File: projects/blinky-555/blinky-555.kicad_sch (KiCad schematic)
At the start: 9 parts, among them J1 9-12V IN, U1 NE555P

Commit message: feat(P1-T9b): fixtures on the parts registry (pins by function, strict mode)
Co-Authored-By: Claude Opus 5.5 <noreply@anthropic.com>
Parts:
- C1: symbol Device:C -> Device:C_Polarized
- D1: LCSC C2895470 -> (none)
- U1: LCSC (none) -> C46749
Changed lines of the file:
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@@
+			)
+		)
+		(property "LCSC" "C46749"
+			(at 48.26 116.84 0)
+			(show_name no)
+			(do_not_autoplace no)
+			(hide yes)
+			(effects
+				(font
+					(size 1.27 1.27)
+				)
 			)
 		)
@@
 	(wire (pts (xy 88.9 115.57) (xy 88.9 118.11)) (stroke (width 0) (type default)))
 	(label "TRIG" (at 88.9 118.11 270) (effects (font (size 1.27 1.27)) (justify right bottom)))
-	(symbol (lib_id "Device:C") (at 101.6 111.76 0) (unit 1) (exclude_from_sim no) (in_bom yes) (on_board yes) (dnp no)
+	(symbol (lib_id "Device:C_Polarized") (at 101.6 111.76 0) (unit 1) (exclude_from_sim no) (in_bom yes) (on_board yes) (dnp no)
 		(property "Reference" "C1"
-			(at 104.902 110.49 0)
+			(at 105.156 110.49 0)
 			(show_name no)
 			(do_not_autoplace no)
@@
 		)
 		(property "Value" "10uF"
-			(at 104.902 113.03 0)
+			(at 105.156 113.03 0)
 			(show_name no)
 			(do_not_autoplace no)
@@
 			)
 		)
-		(property "Description" "Unpolarized capacitor"
+		(property "Description" "Polarized capacitor"
 			(at 101.6 111.76 0)
 			(show_name no)
@@
 			(at 50.8 170.18 0)
 			(show_name no)
-			(do_not_autoplace no)
-			(hide yes)
-			(effects
-				(font
-					(size 1.27 1.27)
-				)
-			)
-		)
-		(property "LCSC" "C2895470"
-			(at 50.8 170.18 0)
-			(show_name no)

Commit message: fix(P1-T9b): keep LCSC ids, package family match, PR-BYNAME
Co-Authored-By: Claude Opus 5.5 <noreply@anthropic.com>
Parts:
- D1: LCSC (none) -> C2895470
- U1: LCSC C46749 -> (none)
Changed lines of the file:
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@@
-			)
-		)
-		(property "LCSC" "C46749"
-			(at 48.26 116.84 0)
-			(show_name no)
-			(do_not_autoplace no)
-			(hide yes)
-			(effects
-				(font
-					(size 1.27 1.27)
-				)
 			)
 		)
@@
 			(at 50.8 170.18 0)
 			(show_name no)
+			(do_not_autoplace no)
+			(hide yes)
+			(effects
+				(font
+					(size 1.27 1.27)
+				)
+			)
+		)
+		(property "LCSC" "C2895470"
+			(at 50.8 170.18 0)
+			(show_name no)

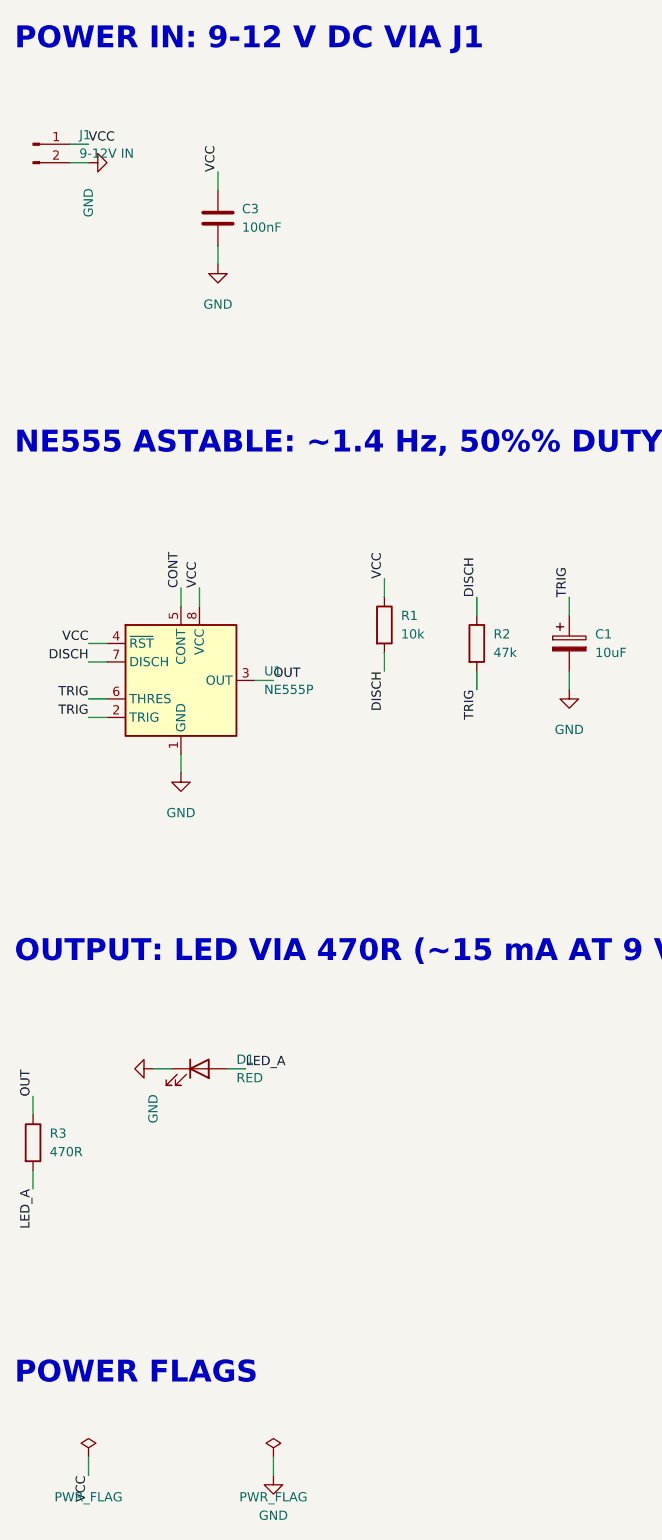
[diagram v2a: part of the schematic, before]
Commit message: feat(P2-T7b): RC-filter recognition, direction severities, expansion class; blinky reverse-polarity diode
Co-Authored-By: Claude Opus 5.5 <noreply@anthropic.com>
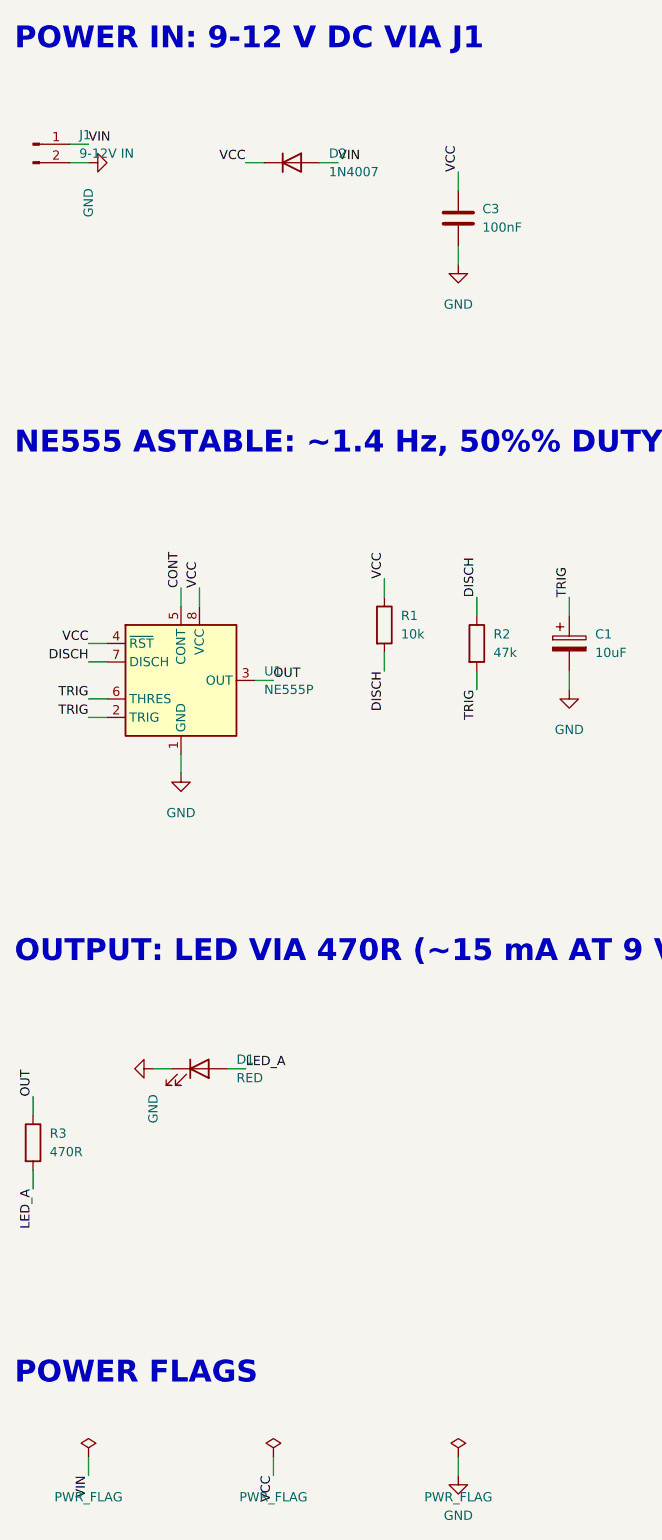
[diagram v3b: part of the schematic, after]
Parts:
- added D2: 1N4007, Diode_THT:D_DO-41_SOD81_P7.62mm_Horizontal, symbol Device:D
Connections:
- net VCC: now also D2.1 (K); no longer J1.1 (Pin_1)
- new net VIN: D2.2 (A), J1.1 (Pin_1)
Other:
- moved on the sheet: C3
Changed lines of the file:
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@@
 	)
 	(wire (pts (xy 33.02 43.18) (xy 35.56 43.18)) (stroke (width 0) (type default)))
-	(label "VCC" (at 35.56 43.18 0) (effects (font (size 1.27 1.27)) (justify left bottom)))
+	(label "VIN" (at 35.56 43.18 0) (effects (font (size 1.27 1.27)) (justify left bottom)))
 	(wire (pts (xy 33.02 45.72) (xy 35.56 45.72)) (stroke (width 0) (type default)))
 	(symbol (lib_id "power:GND") (at 35.56 45.72 90) (unit 1) (exclude_from_sim no) (in_bom no) (on_board yes) (dnp no)
@@
 		(instances (project "blinky-555" (path "/5f01663b-fc79-577d-9212-5270d9429f25" (reference "#PWR001") (unit 1))))
 	)
-	(symbol (lib_id "Device:C") (at 53.34 53.34 0) (unit 1) (exclude_from_sim no) (in_bom yes) (on_board yes) (dnp no)
+	(symbol (lib_id "Device:D") (at 63.5 45.72 0) (unit 1) (exclude_from_sim no) (in_bom yes) (on_board yes) (dnp no)
+		(property "Reference" "D2"
+			(at 68.58 44.45 0)
+			(show_name no)
+			(do_not_autoplace no)
+			(effects
+				(font
+					(size 1.27 1.27)
+				)
+				(justify left)
+			)
+		)
+		(property "Value" "1N4007"
+			(at 68.58 46.99 0)
+			(show_name no)
+			(do_not_autoplace no)
+			(effects
+				(font
+					(size 1.27 1.27)
+				)
+				(justify left)
+			)
+		)
+		(property "Footprint" "Diode_THT:D_DO-41_SOD81_P7.62mm_Horizontal"
+			(at 63.5 45.72 0)
+			(show_name no)
+			(do_not_autoplace no)
+			(hide yes)
+			(effects
+				(font
+					(size 1.27 1.27)
+				)
+			)
+		)
+		(property "Datasheet" ""
+			(at 63.5 45.72 0)
+			(show_name no)
+			(do_not_autoplace no)
+			(hide yes)
+			(effects
+				(font
+					(size 1.27 1.27)
+				)
+			)
+		)
+		(property "Description" "Diode"
+			(at 63.5 45.72 0)
+			(show_name no)
+			(do_not_autoplace no)
+			(hide yes)
+			(effects
+				(font
+					(size 1.27 1.27)
+				)
+			)
+		)
+		(property "Sim.Device" "D"
+			(at 63.5 45.72 0)
+			(show_name no)
+			(do_not_autoplace no)
+			(hide yes)
+			(effects
+				(font
+					(size 1.27 1.27)
+				)
+			)
+		)
+		(property "Sim.Pins" "1=K 2=A"
+			(at 63.5 45.72 0)
+			(show_name no)
+			(do_not_autoplace no)
+			(hide yes)
+			(effects
+				(font
+					(size 1.27 1.27)
+				)
+			)
+		)
+		(property "ki_keywords" "diode"
+			(at 63.5 45.72 0)
+			(show_name no)
+			(do_not_autoplace no)
+			(hide yes)
+			(effects
+				(font
+					(size 1.27 1.27)
+				)
+			)
+		)
+		(pin "1")
+		(pin "2")
+		(instances (project "blinky-555" (path "/5f01663b-fc79-577d-9212-5270d9429f25" (reference "D2") (unit 1))))
+	)
+	(wire (pts (xy 59.69 45.72) (xy 57.15 45.72)) (stroke (width 0) (type default)))
+	(label "VCC" (at 57.15 45.72 180) (effects (font (size 1.27 1.27)) (justify right bottom)))
+	(wire (pts (xy 67.31 45.72) (xy 69.85 45.72)) (stroke (width 0) (type default)))
+	(label "VIN" (at 69.85 45.72 0) (effects (font (size 1.27 1.27)) (justify left bottom)))
+	(symbol (lib_id "Device:C") (at 86.36 53.34 0) (unit 1) (exclude_from_sim no) (in_bom yes) (on_board yes) (dnp no)
 		(property "Reference" "C3"
-			(at 56.642 52.07 0)
+			(at 89.662 52.07 0)
 			(show_name no)
 			(do_not_autoplace no)
@@
 		)
 		(property "Value" "100nF"
-			(at 56.642 54.61 0)
+			(at 89.662 54.61 0)
 			(show_name no)
 			(do_not_autoplace no)
@@
 		)
 		(property "Footprint" "Capacitor_THT:C_Disc_D5.0mm_W2.5mm_P5.00mm"
-			(at 53.34 53.34 0)
-			(show_name no)
-			(do_not_autoplace no)
-			(hide yes)
-			(effects
-				(font
-					(size 1.27 1.27)
-				)
-			)
-		)
-		(property "Datasheet" ""
-			(at 53.34 53.34 0)
+			(at 86.36 53.34 0)
+			(show_name no)
+			(do_not_autoplace no)
+			(hide yes)
+			(effects
+				(font
+					(size 1.27 1.27)
+				)
+			)
+		)
+		(property "Datasheet" ""
+			(at 86.36 53.34 0)
 			(show_name no)
 			(do_not_autoplace no)
@@
 		)
 		(property "Description" "Unpolarized capacitor"
-			(at 53.34 53.34 0)
+			(at 86.36 53.34 0)
 			(show_name no)
 			(do_not_autoplace no)
@@
 		)
 		(property "ki_keywords" "cap capacitor"
-			(at 53.34 53.34 0)
+			(at 86.36 53.34 0)
 			(show_name no)
 			(do_not_autoplace no)
@@
 		(instances (project "blinky-555" (path "/5f01663b-fc79-577d-9212-5270d9429f25" (reference "C3") (unit 1))))
 	)
-	(wire (pts (xy 53.34 49.53) (xy 53.34 46.99)) (stroke (width 0) (type default)))
-	(label "VCC" (at 53.34 46.99 90) (effects (font (size 1.27 1.27)) (justify left bottom)))
-	(wire (pts (xy 53.34 57.15) (xy 53.34 59.69)) (stroke (width 0) (type default)))
-	(symbol (lib_id "power:GND") (at 53.34 59.69 0) (unit 1) (exclude_from_sim no) (in_bom no) (on_board yes) (dnp no)
+	(wire (pts (xy 86.36 49.53) (xy 86.36 46.99)) (stroke (width 0) (type default)))
+	(label "VCC" (at 86.36 46.99 90) (effects (font (size 1.27 1.27)) (justify left bottom)))
+	(wire (pts (xy 86.36 57.15) (xy 86.36 59.69)) (stroke (width 0) (type default)))
+	(symbol (lib_id "power:GND") (at 86.36 59.69 0) (unit 1) (exclude_from_sim no) (in_bom no) (on_board yes) (dnp no)
 		(property "Reference" "#PWR002"
-			(at 53.34 63.19 0)
+			(at 86.36 63.19 0)
 			(show_name no)
 			(do_not_autoplace no)
@@
 		)
 		(property "Value" "GND"
-			(at 53.34 65.19 0)
+			(at 86.36 65.19 0)
 			(show_name no)
 			(do_not_autoplace no)
@@
 		)
 		(property "Footprint" ""
-			(at 53.34 59.69 0)
-			(show_name no)
-			(do_not_autoplace no)
-			(hide yes)
-			(effects
-				(font
-					(size 1.27 1.27)
-				)
-			)
-		)
-		(property "Datasheet" ""
-			(at 53.34 59.69 0)
+			(at 86.36 59.69 0)
+			(show_name no)
+			(do_not_autoplace no)
+			(hide yes)
+			(effects
+				(font
+					(size 1.27 1.27)
+				)
+			)
+		)
+		(property "Datasheet" ""
+			(at 86.36 59.69 0)
 			(show_name no)
 			(do_not_autoplace no)
@@
 		)
 		(property "Description" "Power symbol creates a global label with name \"GND\" , ground"
-			(at 53.34 59.69 0)
+			(at 86.36 59.69 0)
 			(show_name no)
 			(do_not_autoplace no)
@@
 		)
 		(property "ki_keywords" "global power"
-			(at 53.34 59.69 0)
+			(at 86.36 59.69 0)
 			(show_name no)
 			(do_not_autoplace no)
@@
 	)
 	(wire (pts (xy 35.56 223.52) (xy 35.56 226.06)) (stroke (width 0) (type default)))
-	(label "VCC" (at 35.56 226.06 270) (effects (font (size 1.27 1.27)) (justify right bottom)))
+	(label "VIN" (at 35.56 226.06 270) (effects (font (size 1.27 1.27)) (justify right bottom)))
 	(symbol (lib_id "power:PWR_FLAG") (at 60.96 223.52 0) (unit 1) (exclude_from_sim no) (in_bom no) (on_board yes) (dnp no)
 		(property "Reference" "#FLG02"
@@
 	)
 	(wire (pts (xy 60.96 223.52) (xy 60.96 226.06)) (stroke (width 0) (type default)))
-	(symbol (lib_id "power:GND") (at 60.96 226.06 0) (unit 1) (exclude_from_sim no) (in_bom no) (on_board yes) (dnp no)
+	(label "VCC" (at 60.96 226.06 270) (effects (font (size 1.27 1.27)) (justify right bottom)))
+	(symbol (lib_id "power:PWR_FLAG") (at 86.36 223.52 0) (unit 1) (exclude_from_sim no) (in_bom no) (on_board yes) (dnp no)
+		(property "Reference" "#FLG03"
+			(at 86.36 227.02 0)
+			(show_name no)
+			(do_not_autoplace no)
+			(hide yes)
+			(effects
+				(font
+					(size 1.27 1.27)
+				)
+			)
+		)
+		(property "Value" "PWR_FLAG"
+			(at 86.36 229.02 0)
+			(show_name no)
+			(do_not_autoplace no)
+			(effects
+				(font
+					(size 1.27 1.27)
+				)
+			)
+		)
+		(property "Footprint" ""
+			(at 86.36 223.52 0)
+			(show_name no)
+			(do_not_autoplace no)
+			(hide yes)
+			(effects
+				(font
+					(size 1.27 1.27)
+				)
+			)
+		)
+		(property "Datasheet" ""
+			(at 86.36 223.52 0)
+			(show_name no)
+			(do_not_autoplace no)
+			(hide yes)
+			(effects
+				(font
+					(size 1.27 1.27)
+				)
+			)
+		)
+		(property "Description" "Special symbol for telling ERC where power comes from"
+			(at 86.36 223.52 0)
+			(show_name no)
+			(do_not_autoplace no)
+			(hide yes)
+			(effects
+				(font
+					(size 1.27 1.27)
+				)
+			)
+		)
+		(property "ki_keywords" "flag power"
+			(at 86.36 223.52 0)
+			(show_name no)
+			(do_not_autoplace no)
+			(hide yes)
+			(effects
+				(font
+					(size 1.27 1.27)
+				)
+			)
+		)
+		(pin "1")
+		(instances (project "blinky-555" (path "/5f01663b-fc79-577d-9212-5270d9429f25" (reference "#FLG03") (unit 1))))
+	)
+	(wire (pts (xy 86.36 223.52) (xy 86.36 226.06)) (stroke (width 0) (type default)))
+	(symbol (lib_id "power:GND") (at 86.36 226.06 0) (unit 1) (exclude_from_sim no) (in_bom no) (on_board yes) (dnp no)
 		(property "Reference" "#PWR007"
-			(at 60.96 229.56 0)
+			(at 86.36 229.56 0)
 			(show_name no)
 			(do_not_autoplace no)
@@
 		)
 		(property "Value" "GND"
-			(at 60.96 231.56 0)
+			(at 86.36 231.56 0)
 			(show_name no)
 			(do_not_autoplace no)
@@
 		)
 		(property "Footprint" ""
-			(at 60.96 226.06 0)
-			(show_name no)
-			(do_not_autoplace no)
-			(hide yes)
-			(effects
-				(font
-					(size 1.27 1.27)
-				)
-			)
-		)
-		(property "Datasheet" ""
-			(at 60.96 226.06 0)
+			(at 86.36 226.06 0)
+			(show_name no)
+			(do_not_autoplace no)
+			(hide yes)
+			(effects
+				(font
+					(size 1.27 1.27)
+				)
+			)
+		)
+		(property "Datasheet" ""
+			(at 86.36 226.06 0)
 			(show_name no)
 			(do_not_autoplace no)
@@
 		)
 		(property "Description" "Power symbol creates a global label with name \"GND\" , ground"
-			(at 60.96 226.06 0)
+			(at 86.36 226.06 0)
 			(show_name no)
 			(do_not_autoplace no)
@@
 		)
 		(property "ki_keywords" "global power"
-			(at 60.96 226.06 0)
-			(show_name no)
-			(do_not_autoplace no)
+			(at 86.36 226.06 0)
+			(show_name no)
+			(do_not_autoplace no)
